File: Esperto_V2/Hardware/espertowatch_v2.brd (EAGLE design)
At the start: 35 x 35 mm, 50 parts, among them J1 SM02B, J2 47346-0001, Q1 DMP2035U, U1 AP2112K-3.3V, U2 MCP73832, U3 MAX1921EUT18+T, U4 ATSAMD21G-A, U5 MAX30102EFD+, U6 MAX14595ETAT, U7 MB85RC256VPF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

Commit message: Added new hardware and EAGLE libraries
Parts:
- moved C13 3.42 mm to (9.26, 23.0), turned to 270 degrees
- moved C12 3.34 mm to (9.23, 25.4)
- moved U1 0.50 mm to (10.7, 10.3)
- moved C7 0.41 mm to (15.1, 26.1), turned to 0 degrees
- moved C5 0.40 mm to (13.4, 10.9)
- moved C4 0.30 mm to (8.12, 11.0)
- moved C10 0.30 mm to (14.4, 10.9)
- moved Y1 0.22 mm to (7.60, 24.4)
- moved C21 0.10 mm to (29.8, 18.5)
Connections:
- net 3V3: now also J3.4; no longer J3.3
- net GND: now also J3.2, J3.7; no longer J3.1, J3.8
- net SCL: now also J3.6; no longer J3.5
- net SDA: now also J3.8; no longer J3.7
- net SWCLK: now also J3.3; no longer J3.4
- net SWDIO: now also J3.1; no longer J3.2
- net SWRST: now also J3.5; no longer J3.6
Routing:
- net SWDIO: track 13.6 -> 2.98 mm
- net GND: track 14.2 -> 23.8 mm, vias 13 -> 54
- net SWRST: track 12.1 -> 4.91 mm
- net 3V3: track 75.7 -> 82.6 mm
- net SWCLK: track 14.3 -> 8.87 mm
- net N$1: track 22.5 -> 18.5 mm
- net SCL: track 34.4 -> 30.8 mm
- net N$6: track 6.01 -> 4.73 mm
- net SDA: track 26.6 -> 27.7 mm
- net N$7: track 5.32 -> 4.35 mm
- net D9_BLE_RST: track 28.7 -> 28.0 mm
- net D11_BLE_MOSI: track 19.5 -> 20.1 mm
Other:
- board text added: "3V3"
- board text added: "BATT"
- board text added: "C1"
- board text added: "C10"
- board text added: "C11"
- board text added: "C12"
- board text added: "C13"
- board text added: "C14"
- board text added: "C15"
- board text added: "C16"
- board text added: "C17"
- board text added: "C18"
- board text added: "C19"
- board text added: "C2"
- board text added: "C20"
- board text added: "C21"
- board text added: "C22"
- board text added: "C3"
- board text added: "C4"
- board text added: "C5"
- board text added: "C6"
- board text added: "C7"
- board text added: "C8"
- board text added: "C9"
- board text added: "CLK"
- board text added: "D1"
- board text added: "DIO"
- board text added: "ESPERTO WATCH"
- board text added: "GND"
- board text added: "J1"
- board text added: "J2"
- board text added: "J3"
- board text added: "L1"
- board text added: "Q1"
- board text added: "R1"
- board text added: "R10"
- board text added: "R11"
- board text added: "R12"
- board text added: "R2"
- board text added: "R3"
- board text added: "R4"
- board text added: "R5"
- board text added: "R6"
- board text added: "R7"
- board text added: "R8"
- board text added: "R9"
- board text added: "RST"
- board text added: "SCL"
- board text added: "SDA"
- board text added: "U1"
- board text added: "U2"
- board text added: "U3"
- board text added: "U4"
- board text added: "U5"
- board text added: "U6"
- board text added: "U7"
- board text added: "U8"
- board text added: "U9"
- board text added: "V2"
- board text added: "Y1"

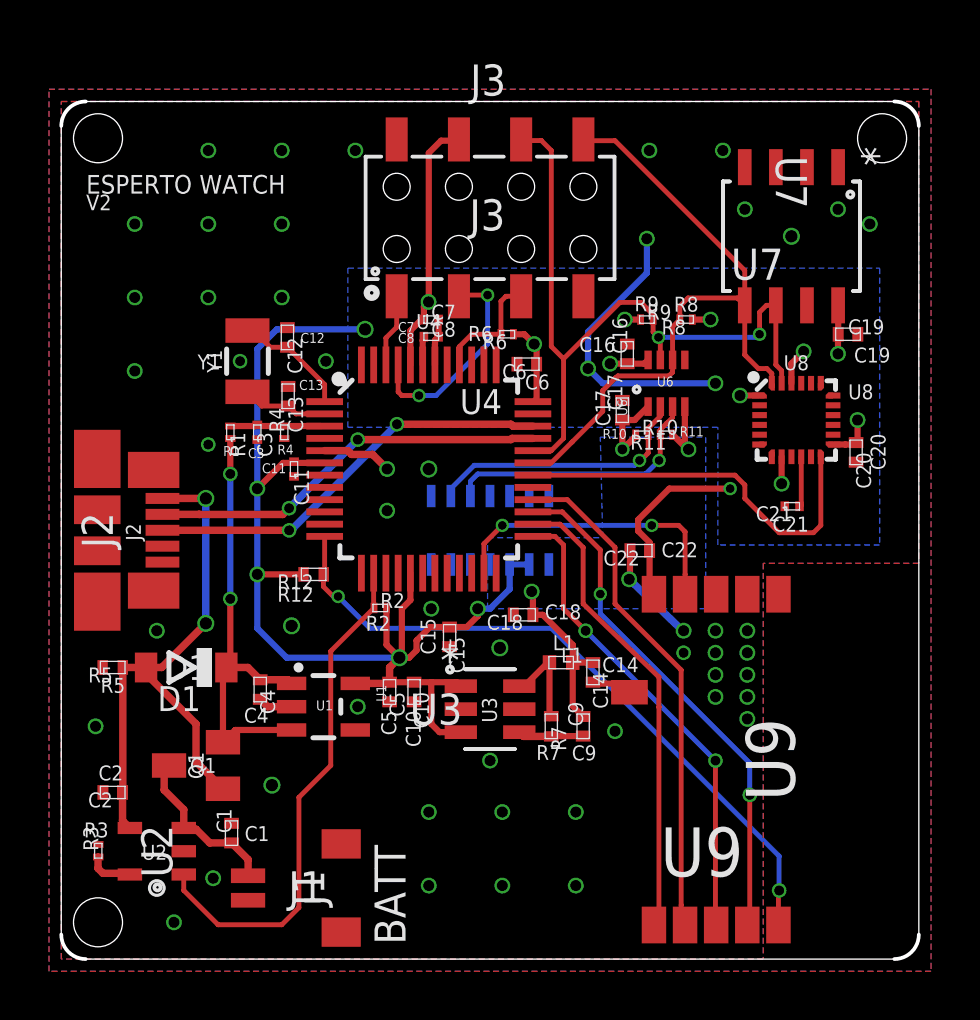
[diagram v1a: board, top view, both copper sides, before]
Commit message: BLE support for APP - bug fixes
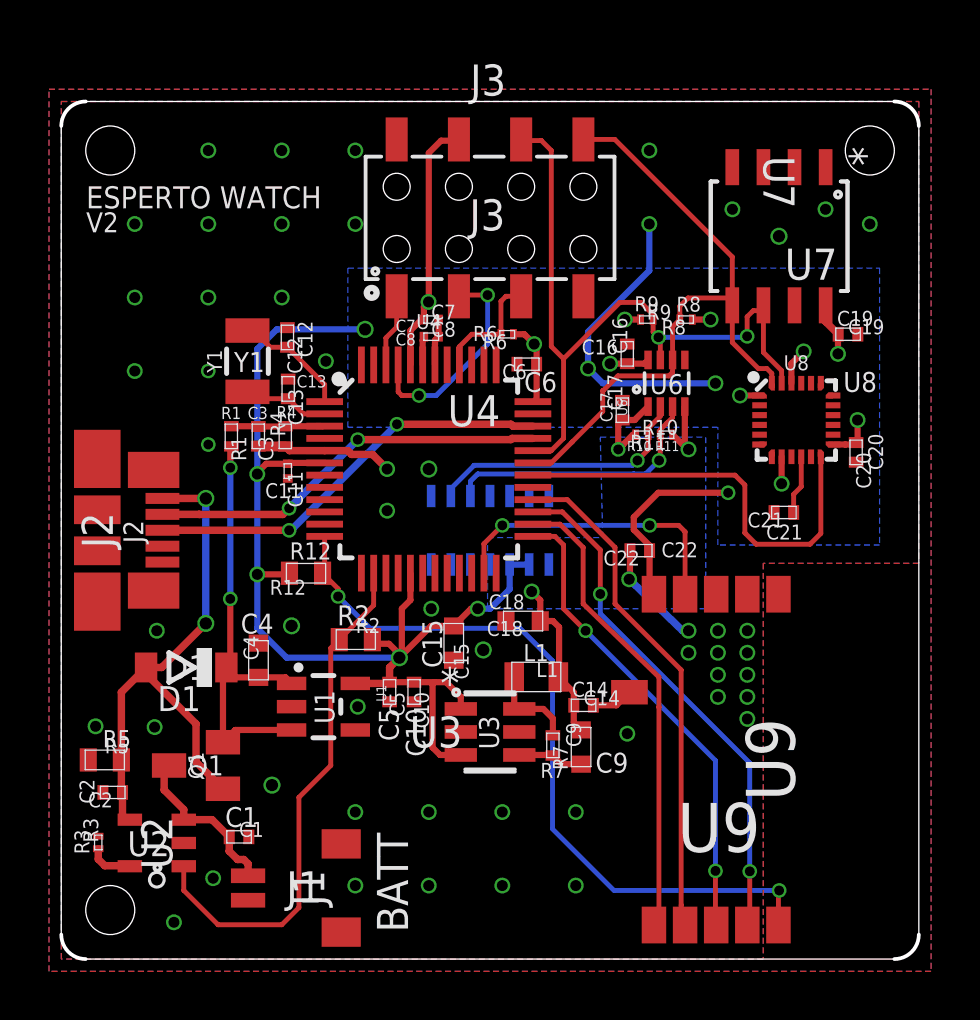
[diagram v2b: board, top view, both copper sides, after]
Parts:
- C15, C18: value 1uF -> 1.0uF; device CAPACITOR:C0402_MURATA_GRM15-GJM15 -> CAPACITOR:C0603_MURATA_GRM18
- C21, C3: device CAPACITOR:C0201_MURATA_GRM03 -> CAPACITOR:C0402_MURATA_GRM15-GJM15
- C4, C9: device CAPACITOR:C0402_MURATA_GRM15-GJM15 -> CAPACITOR:C0603_MURATA_GRM18
- L1: device INDUCTOR:L0402_MURATA_LQP15_LQG15 -> INDUCTOR:L0805_TDK_MLZ
- R1, R4: device RESISTOR:R0201_VISHAY_CRCW0201 -> RESISTOR:R0402_VISHAY_CRCW0402
- R12, R5: device RESISTOR:R0402_VISHAY_CRCW0402 -> RESISTOR:R0603_VISHAY_MCT0603
- R2: device RESISTOR:R0201_VISHAY_CRCW0201 -> RESISTOR:R0603_VISHAY_MCT0603
- U3: value MAX1921EUT18+T -> MAX1921EUT18+
- U6: value MAX14595ETAT -> MAX14595ETA+
- moved R5 3.79 mm to (1.78, 8.13), turned to 0 degrees
- moved R2 1.63 mm to (12.0, 13.0)
- moved C14 1.40 mm to (21.3, 10.4), turned to 0 degrees
- moved C4 1.20 mm to (8.05, 12.2), turned to 90 degrees
- moved L1 1.17 mm to (19.4, 11.5)
- moved U3 0.93 mm to (17.5, 9.27)
- moved C9 0.85 mm to (21.2, 8.65)
- moved R7 0.78 mm to (20.1, 8.72)
- moved U7 0.51 mm to (29.3, 29.5)
- moved C21 0.42 mm to (29.5, 18.2)
- moved C1 0.34 mm to (7.26, 4.99), turned to 0 degrees
- moved R3 0.34 mm to (1.51, 4.76)
- moved U2 0.34 mm to (3.90, 4.74)
- moved R12 0.31 mm to (9.99, 15.7)
- moved C15 0.31 mm to (16.0, 12.9)
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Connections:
- net GND: now also R5.1; no longer R5.2
- net VUSB: now also R5.2; no longer R5.1
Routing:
- net D9_BLE_RST: track 28.0 -> 31.2 mm
- net GND: track 23.8 -> 26.5 mm, vias 54 -> 56
- net D7_MPU_INT: track 15.9 -> 17.3 mm
- net N$7: track 4.35 -> 3.52 mm
- net SDA: track 27.7 -> 27.0 mm
- net VUSB: track 24.0 -> 23.4 mm
- net N$10: track 4.20 -> 3.61 mm

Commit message: Removed I2C pullups
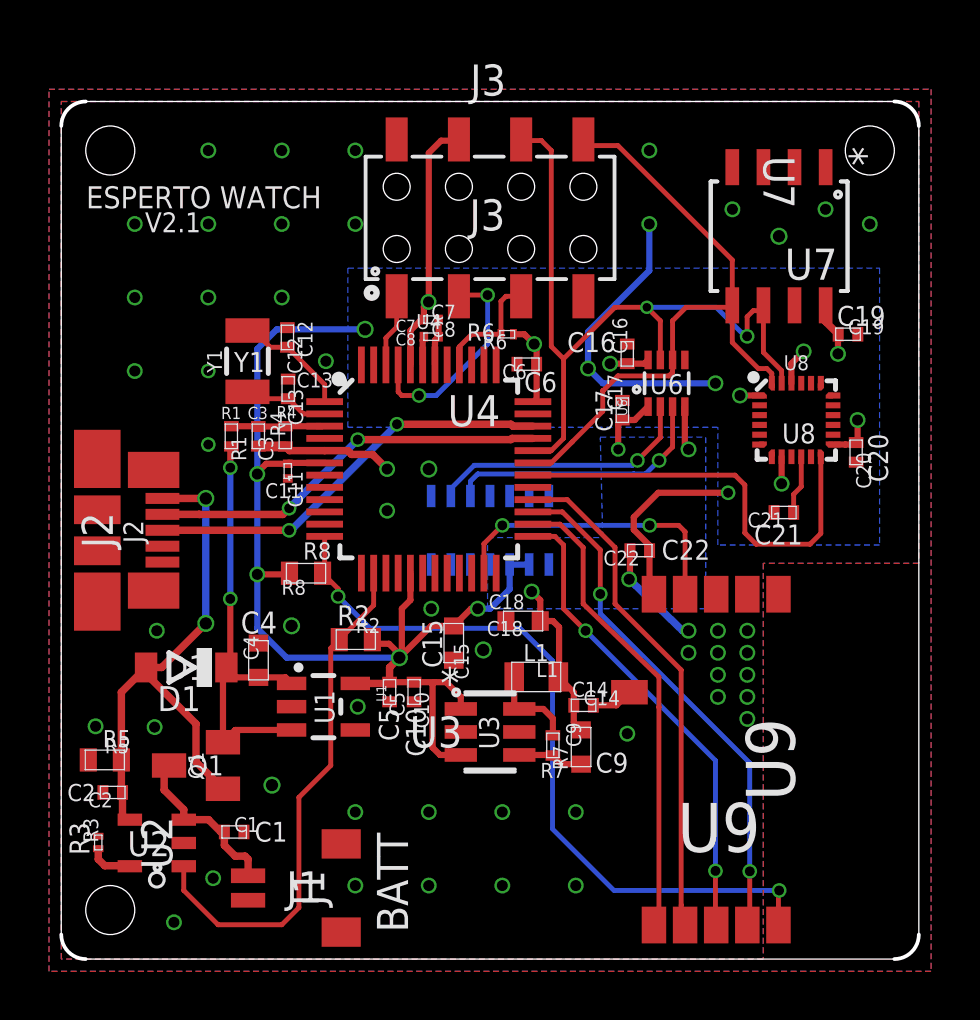
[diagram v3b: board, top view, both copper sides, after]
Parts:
- removed R10, R11, R9: 4.7k, RESISTOR:R0201_VISHAY_CRCW0201
- removed R12: 100k, RESISTOR:R0603_VISHAY_MCT0603
- R8: value 4.7k -> 100k; device RESISTOR:R0201_VISHAY_CRCW0201 -> RESISTOR:R0603_VISHAY_MCT0603
- moved R8 18.6 mm to (9.99, 15.7)
- moved C1 0.28 mm to (7.06, 5.19)
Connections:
- net 1V8: no longer R10.1, R11.1
- net 3V3: now also R8.2; no longer R12.2, R8.1, R9.1
- net D9_BLE_RST: now also R8.1; no longer R12.1
- net N$16: no longer R10.2
- net N$17: no longer R11.2
- net SCL: no longer R9.2
- net SDA: no longer R8.2
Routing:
- net 1V8: track 13.4 -> 11.2 mm
- net 3V3: track 82.7 -> 81.3 mm, vias 16 -> 14
- net SCL: track 30.8 -> 31.6 mm
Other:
- board text added: "V2.1"
- board text removed: "R10"
- board text removed: "R11"
- board text removed: "R12"
- board text removed: "R9"
- board text removed: "V2"
